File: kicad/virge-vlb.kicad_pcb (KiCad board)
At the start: 4 copper layers, 240.5 x 69.4 mm, 96 parts, among them J1 VLB_slot, J2 VGA, U1 74LS244, U2 27C020, U7 86C325, U8 7404, U9 7408, Y1 14.318MHz

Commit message: some improvements here and there
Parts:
- removed the C9 at (71.5, 94.5)
- C10: value 10pF -> 100nF
- moved C10 117.8 mm to (183.6, 115.2), turned to 0 degrees
- moved Y1 6.21 mm to (72.6, 96.5)
- moved C25 5.76 mm to (164.8, 86.0)
- moved R21 0.16 mm to (97.1, 95.8)
- moved R20 0.15 mm to (99.2, 95.8)
- renumbered C19 to C9
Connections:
- C10 pad 2: Net-(U7H-XOUT) -> VCC
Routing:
- net Net-(U7H-XIN): track 15.7 -> 6.69 mm
- net Net-(U7H-XOUT): track 19.2 -> 10.7 mm
- net /S3_RED: track 193.7 -> 190.7 mm
- net /S3_BLUE: track 183.0 -> 180.3 mm
- net /S3_GREEN: track 188.3 -> 185.7 mm
- net VCC: track 144.5 -> 147.0 mm
- net GND: track 164.7 -> 166.2 mm, vias 221 -> 225
- net /BLUE: track 24.0 -> 25.2 mm
- net /Memory Bus/WE: track 121.1 -> 120.2 mm
- net /VL Bus/IRQ9: track 70.2 -> 69.5 mm
- net /RED: track 13.7 -> 14.4 mm
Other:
- board text added: "- 10pF: C1 -> C8 - 100nF: C11 -> C18 - 10uF: C20 -> C29 - 1nF: C19"
- board text removed: "- 10pF: C1 -> C10 - 100nF: C11 -> C18 - 10uF: C20 -> C29 - 1nF: C19"

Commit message: added vbios
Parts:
- moved R7 1.30 mm to (191.0, 112.8)
- moved C16 0.33 mm to (117.1, 123.6)
- moved R39 0.21 mm to (160.6, 123.4)
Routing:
- net /ISA Bus/R_A14: track 37.7 -> 35.1 mm
- net /ISA Bus/R_A10: track 58.6 -> 56.2 mm
- net Net-(U7F-~{CAS1}): track 66.7 -> 64.4 mm
- net /Memory Bus/MA8: track 145.8 -> 144.0 mm
- net /Memory Bus/PD35: track 21.2 -> 20.2 mm
- net /ISA Bus/R_A9: track 50.9 -> 51.7 mm
- net /Memory Bus/MA1: track 152.7 -> 152.0 mm
- net /Memory Bus/MA3: track 158.8 -> 158.1 mm
- net GND: track 166.2 -> 166.9 mm, vias 225 -> 224
- net /Memory Bus/MA2: track 155.0 -> 154.3 mm
- net /Memory Bus/MA0: track 149.4 -> 148.7 mm
- net /ISA Bus/R_A11: track 52.3 -> 52.9 mm
- net VCC: track 147.0 -> 147.5 mm
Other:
- board text removed: "more Config"

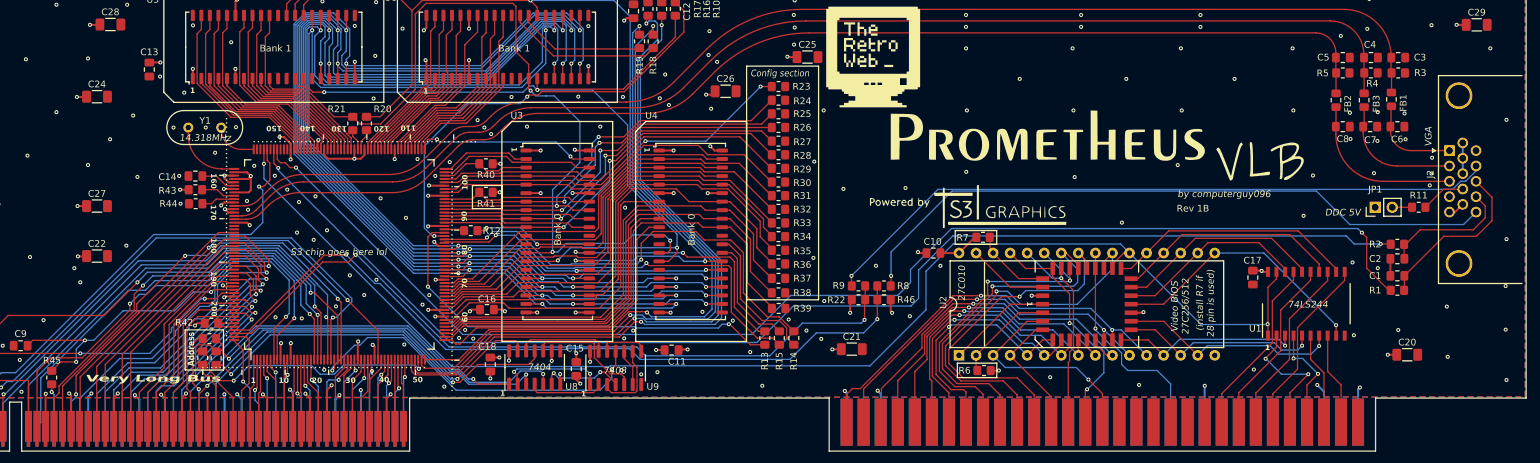
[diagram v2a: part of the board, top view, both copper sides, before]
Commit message: some optimizations and silkscreen updating
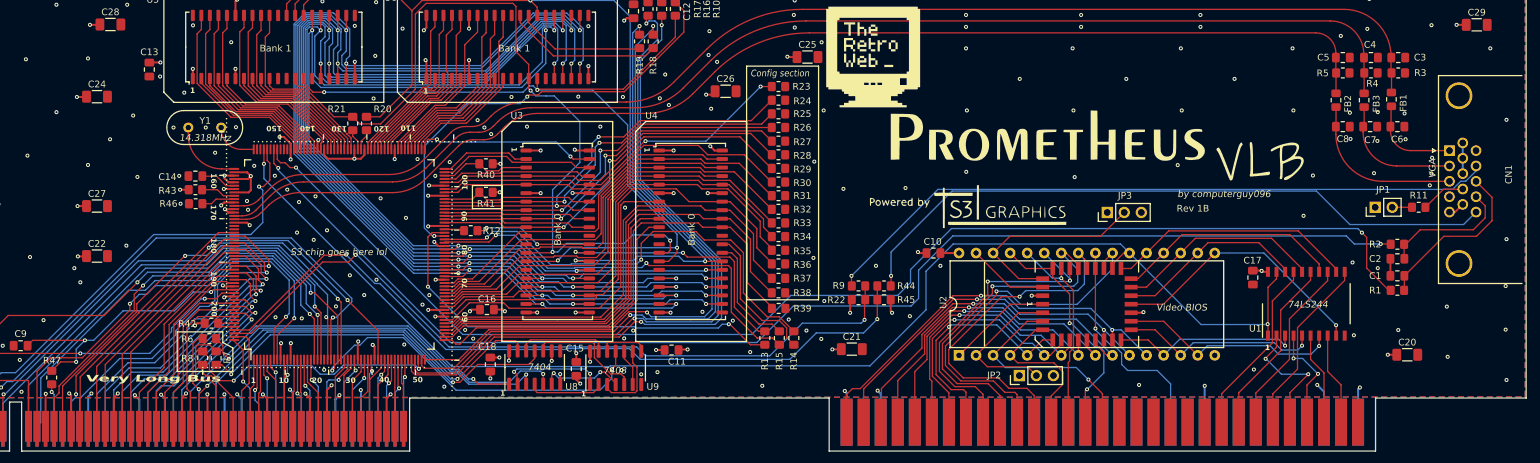
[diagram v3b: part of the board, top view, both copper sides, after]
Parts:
- removed the R6 at (191.2, 132.7)
- removed the R7 at (191.0, 112.8)
- added JP2: Conn_01x03, Connector_PinHeader_2.54mm:PinHeader_1x03_P2.54mm_Vertical, F.Cu at (196.4, 133.4)
- added JP3: Conn_01x03, Connector_PinHeader_2.54mm:PinHeader_1x03_P2.54mm_Vertical, F.Cu at (209.5, 109.1)
- C9: value 1nF -> 100pF
- JP1: value DDC 5V -> Conn_01x02
- R13: value 3 x 33R -> 33R
- R20: value 2 x 33R -> 33R
- R23: value 10K each -> 10K
- R47: renamed from R45; value 100R -> 150R
- R6: renamed from R47; value 0 -> 0R
- R7: renamed from R48; value 0 -> 0R
- R8: renamed from R49; value 0 -> 0R
- U3, U4, U5, U6: value ~ -> V53C16258H
- renumbered J2 to CN1, R8 to R44, R46 to R45, R44 to R46
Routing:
- net Net-(JP3-Pin_2): track 11.5 -> 31.6 mm
- net Net-(JP2-Pin_2): track 14.9 -> 22.8 mm
- net VCC: track 147.5 -> 142.8 mm, vias 57 -> 56
- net /ISA Bus/R_A12: track 18.9 -> 23.6 mm
- net GND: vias 224 -> 222
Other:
- board text added: "- 10K: R22 -> R43 - 33R: R1, R2, R9 -> R22 - 75R: R3, R4, R5 - 4.7K: R44, R45 - 150R: R46, R47 - 0R: R6, R7, R8"
- board text added: "1-2 any 2-3 2-3 1-2 2-3 2-3 1-2 1-2 1-2"
- board text added: "1GB (default)"
- board text added: "28 pin 32 pin (A) 32 pin (B) 32 pin (C) 32 pin (D)"
- board text added: "A - 00000h -> 0FFFFh B - 10000h -> 1FFFFh C - 20000h -> 2FFFFh D - 30000h -> 3FFFFh"
- board text added: "Address location: (0R)"
- board text added: "CAS/OE"
- board text added: "Configuration resistors"
- board text added: "EEPROM type:"
- board text added: "JP2 JP3"
- board text added: "Jumper settings"
- board text added: "Mem size"
- board text added: "Mem type"
- board text added: "Monitor DDC (JP1):"
- board text added: "OFF (default) ON - R23 (RAMDAC Write Snooping) disabled enabled - R24 (VBIOS size) 27C256 27C512 - R25 (VBIOS access) enabled disabled - R33 (RAS low timing delay) 3.5MCLKs 4.5MCLKs - R35 (RAS pre-charge delay) 2.5MCLKs 3.5MCLKs - R37 (Serial I/O type) MMIO only MMIO + FF20h - R38 (Serial I/O address) 000E2h 000E8h - R41 (Clock source) internal external"
- board text added: "OFF - don't supply 5V"
- board text added: "ON - supply 5V to monitor"
- board text added: "R26 R27 R28 - 1MB ON OFF OFF - 2MB ON ON OFF"
- board text added: "R29 R30 1-cycle EDO ON ON Reserved OFF ON 2-cycle EDO ON OFF fast page OFF OFF"
- board text added: "R31 R32 - no adj. OFF OFF - 3.5ns ON OFF - 5ns OFF ON - 6.5ns ON ON"
- board text added: "R6"
- board text added: "R7"
- board text added: "R8"
- board text added: "VBIOS address location:"
- board text added: "Video BIOS"
- board text added: "Video chip registers (10K):"
- board text removed: "(install R7 if 28 pin is used)"
- board text removed: "- 10K: R22 -> R43 - 33R: R1, R2, R9 -> R22 - 75R: R3, R4, R5 - 4.7K: R8, R46 - 150R: R44 - 100R: R45 - 0R: R6, R7 + address box"
- board text removed: "1GB"
- board text removed: "27C010"
- board text removed: "Address"
- board text removed: "Address location:"
- board text removed: "Video BIOS 27C256/512"
